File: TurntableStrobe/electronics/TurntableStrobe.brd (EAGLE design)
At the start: 25.1 x 17.8 mm, 15 parts, among them IC1 TINY25, J1 ISP, Q1 12MHz

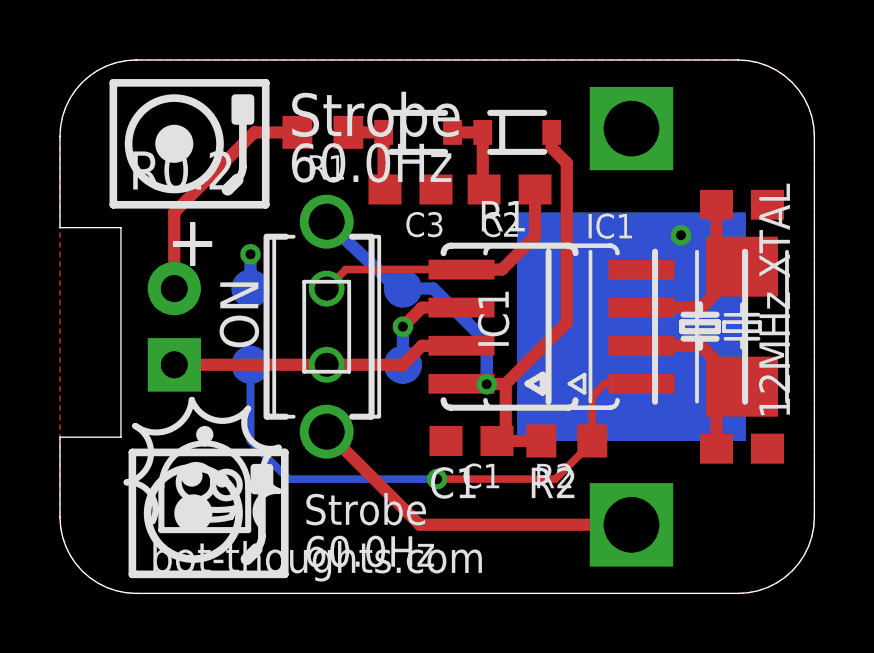
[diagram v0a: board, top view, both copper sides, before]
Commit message: Fix for ISP (AVR910). Minor silk change.
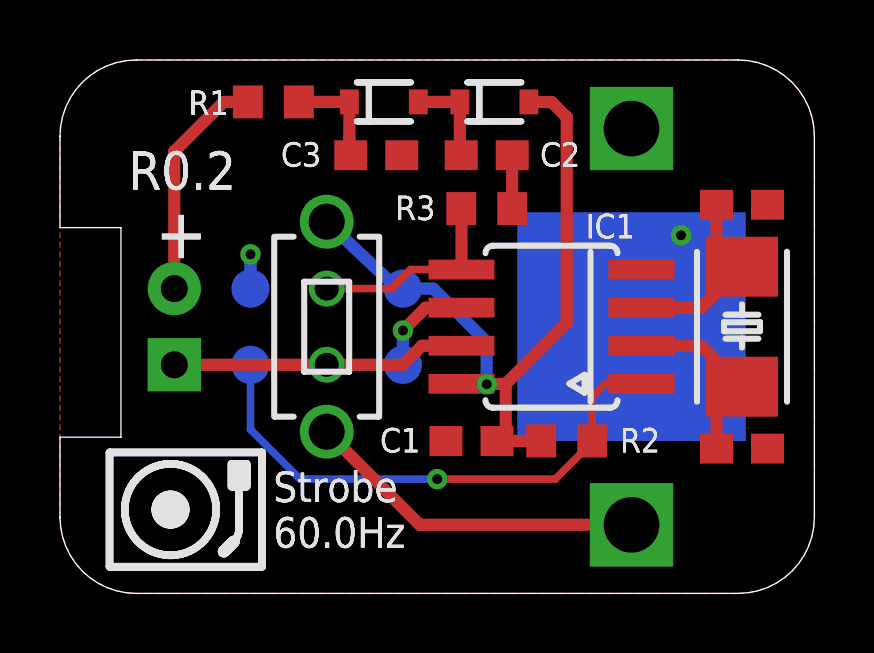
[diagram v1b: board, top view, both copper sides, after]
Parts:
- added R3: 100, rcl:R0603
- moved R1 1.94 mm to (7.11, 16.4)
- moved C3 1.62 mm to (10.5, 14.6)
- moved D2 1.53 mm to (10.8, 16.4)
- moved C2 1.37 mm to (14.2, 14.6)
- moved D1 1.27 mm to (14.5, 16.4)
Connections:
- net N$1 renamed VBAT
- new net N$4: C2.2, R3.1
- net PB0: now also R3.2; no longer C2.2
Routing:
- net PB0: track 9.23 -> 6.79 mm
- net N$4: track 0.00 -> 1.78 mm
- net VCC: track 22.8 -> 24.6 mm
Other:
- board text added: "C2"
- board text added: "C3"
- board text added: "R3"
- board text removed: "12MHz XTAL"
- board text removed: "ON"

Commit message: Revise diode footprint
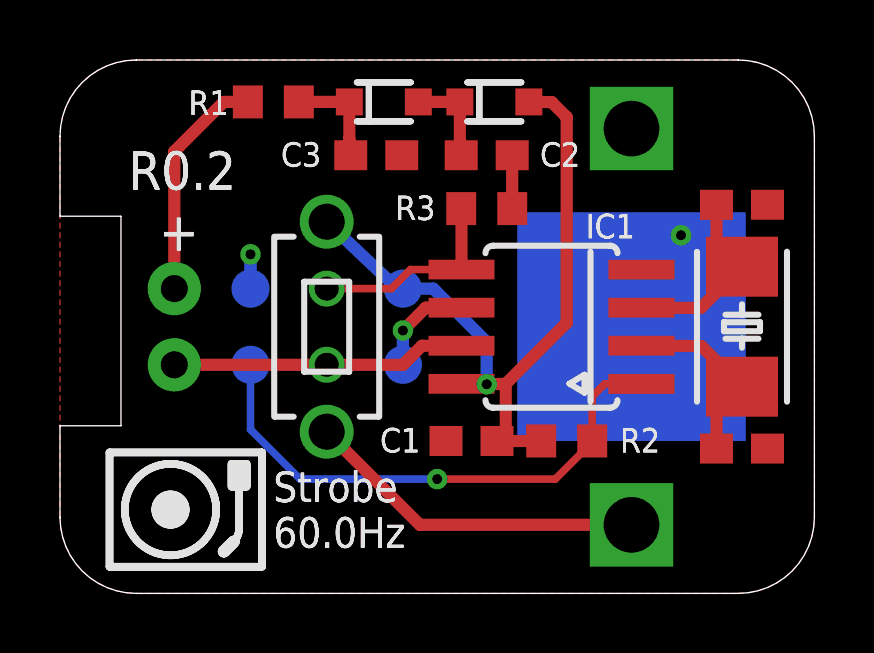
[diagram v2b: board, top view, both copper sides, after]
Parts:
- D1, D2: value (none) -> DIODE_SOD323; device SparkFun-DiscreteSemi:SOD-323 -> bt_diode:SOD-323
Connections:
- net N$2: now also D1.C, D2.A; no longer D1.1, D2.2
- net VCC: now also D1.A; no longer D1.2
- net VHI: now also D2.C; no longer D2.1
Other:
- outline, holes or cut-outs redrawn
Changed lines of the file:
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@@
 <wire x1="22.606" y1="17.78" x2="2.54" y2="17.78" width="0" layer="20"/>
 <wire x1="2.54" y1="17.78" x2="0" y2="15.24" width="0" layer="20" curve="90"/>
-<wire x1="0" y1="15.24" x2="0" y2="12.192" width="0" layer="20"/>
-<wire x1="0" y1="5.207" x2="0" y2="2.54" width="0" layer="20"/>
+<wire x1="0" y1="15.24" x2="0" y2="12.573" width="0" layer="20"/>
+<wire x1="0" y1="5.588" x2="0" y2="2.54" width="0" layer="20"/>
 <wire x1="0" y1="2.54" x2="2.54" y2="0" width="0" layer="20" curve="90"/>
 <wire x1="2.54" y1="0" x2="22.606" y2="0" width="0" layer="20"/>
 <wire x1="22.606" y1="0" x2="25.146" y2="2.54" width="0" layer="20" curve="90"/>
 <text x="15.827" y="16.051" size="1.016" layer="26" font="vector" rot="MR0">bot-thoughts.com</text>
-<text x="3.175" y="11.176" size="1.6764" layer="25" font="vector" ratio="16">+</text>
 <text x="7.112" y="3.048" size="1.016" layer="25" font="vector" ratio="10">Strobe</text>
-<wire x1="2.032" y1="12.192" x2="0" y2="12.192" width="0" layer="20"/>
-<wire x1="2.032" y1="12.192" x2="2.032" y2="5.207" width="0" layer="20"/>
-<wire x1="2.032" y1="5.207" x2="0" y2="5.207" width="0" layer="20"/>
+<wire x1="2.032" y1="12.573" x2="0" y2="12.573" width="0" layer="20"/>
+<wire x1="2.032" y1="12.573" x2="2.032" y2="5.588" width="0" layer="20"/>
+<wire x1="2.032" y1="5.588" x2="0" y2="5.588" width="0" layer="20"/>
 <polygon width="0.254" layer="22">
 <vertex x="4.224565625" y="2.358009375" curve="-9.500008"/>
@@
 <wire x1="17.482996875" y1="6.690003125" x2="17.482996875" y2="7.290003125" width="0.2032" layer="121"/>
 <wire x1="17.482996875" y1="7.290003125" x2="16.983" y2="6.990003125" width="0.2032" layer="121"/>
+<text x="3.302" y="11.43" size="1.27" layer="121" font="vector" ratio="16">+</text>
 <wire x1="24.232996875" y1="11.38999375" x2="24.232996875" y2="6.39000625" width="0.2032" layer="121"/>
 <wire x1="21.233003125" y1="6.39000625" x2="21.233003125" y2="11.38999375" width="0.2032" layer="121"/>
@@
 <vertex x="4.55261875" y="3.15000625"/>
 </polygon>
-<text x="3.175" y="11.176" size="1.6764" layer="121" font="vector" ratio="16">+</text>
 <text x="7.112" y="3.048" size="1.016" layer="121" font="vector" ratio="20">Strobe</text>
 <text x="7.112" y="1.524" size="1.016" layer="121" font="vector" ratio="20">60.0Hz</text>
@@
 <attribute name="NAME" x="7.366" y="14.224" size="0.8128" layer="25" font="vector" ratio="10"/>
 </element>
-<element name="D1" library="SparkFun-DiscreteSemi" package="SOD-323" value="" x="14.478" y="16.383" smashed="yes">
-<attribute name="PROD_ID" value="DIO-09646" x="14.478" y="16.383" size="1.27" layer="27" ratio="16" display="off"/>
-<attribute name="VALUE" x="13.462" y="14.986" size="0.4064" layer="27"/>
-</element>
-<element name="D2" library="SparkFun-DiscreteSemi" package="SOD-323" value="" x="10.795" y="16.383" smashed="yes">
-<attribute name="PROD_ID" value="DIO-09646" x="10.795" y="16.383" size="1.27" layer="27" ratio="16" display="off"/>
-<attribute name="VALUE" x="9.779" y="14.986" size="0.4064" layer="27"/>
-</element>
+<element name="D1" library="bt_diode" package="SOD-323" value="DIODE_SOD323" x="14.478" y="16.383" smashed="yes"/>
+<element name="D2" library="bt_diode" package="SOD-323" value="DIODE_SOD323" x="10.795" y="16.383" smashed="yes"/>
 <element name="R3" library="rcl" package="R0603" value="100" x="14.224" y="12.827" smashed="yes" rot="R180">
 <attribute name="NAME" x="11.176" y="12.446" size="0.8128" layer="25" font="vector" ratio="10"/>
@@
 <wire x1="11.43" y1="10.16" x2="11.247" y2="10.16" width="0.4064" layer="16"/>
 <wire x1="11.247" y1="10.16" x2="8.89" y2="12.39" width="0.4064" layer="16"/>
-<contactref element="D1" pad="2"/>
+<contactref element="D1" pad="A"/>
 <wire x1="15.628" y1="16.383" x2="16.39" y2="16.376" width="0.4064" layer="1"/>
 <wire x1="16.39" y1="16.376" x2="16.891" y2="15.875" width="0.4064" layer="1"/>
@@
 <signal name="VHI">
 <contactref element="C3" pad="1"/>
-<contactref element="D2" pad="1"/>
+<contactref element="D2" pad="C"/>
 <contactref element="R1" pad="1"/>
 <wire x1="9.645" y1="16.383" x2="7.962" y2="16.383" width="0.4064" layer="1"/>
@@
 <signal name="N$2">
 <contactref element="C2" pad="1"/>
-<contactref element="D1" pad="1"/>
-<contactref element="D2" pad="2"/>
+<contactref element="D1" pad="C"/>
+<contactref element="D2" pad="A"/>
 <wire x1="11.945" y1="16.383" x2="13.328" y2="16.383" width="0.4064" layer="1"/>
 <wire x1="13.328" y1="16.383" x2="13.328" y2="15.032" width="0.4064" layer="1"/>

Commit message: Change diode value to specify 1N4148
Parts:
- D1, D2: value DIODE_SOD323 -> 1N4148
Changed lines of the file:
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@@
 <attribute name="NAME" x="7.366" y="14.224" size="0.8128" layer="25" font="vector" ratio="10"/>
 </element>
-<element name="D1" library="bt_diode" package="SOD-323" value="DIODE_SOD323" x="14.478" y="16.383" smashed="yes"/>
-<element name="D2" library="bt_diode" package="SOD-323" value="DIODE_SOD323" x="10.795" y="16.383" smashed="yes"/>
+<element name="D1" library="bt_diode" package="SOD-323" value="1N4148" x="14.478" y="16.383" smashed="yes"/>
+<element name="D2" library="bt_diode" package="SOD-323" value="1N4148" x="10.795" y="16.383" smashed="yes"/>
 <element name="R3" library="rcl" package="R0603" value="100" x="14.224" y="12.827" smashed="yes" rot="R180">
 <attribute name="NAME" x="11.176" y="12.446" size="0.8128" layer="25" font="vector" ratio="10"/>
